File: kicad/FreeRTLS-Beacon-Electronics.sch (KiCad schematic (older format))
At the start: 28 parts

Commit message: Annotate sch
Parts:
- gave numbers to parts that had none: 28

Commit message: Add ferrite and change lib to fix ERC errors
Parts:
- added L4: L, symbol Device:L
- U3: symbol RF_Module:DWM1001 -> FreeRTLS-Beacon:DWM1001
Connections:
- wire segments 126 -> 130
- no-connect marks 52 -> 53
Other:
- moved on the sheet: C5, C6, D2, D4, J1, L1
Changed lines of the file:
@@
 $EndDescr
 $Comp
-L RF_Module:DWM1001 U3
+L FreeRTLS-Beacon:DWM1001 U3
 U 1 1 5F4EAC7B
 P 8600 3650
@@
 L Connector:USB_B_Micro J1
 U 1 1 5F4ED800
-P 900 1200
-F 0 "J1" H 957 1667 50  0000 C CNN
-F 1 "USB_B_Micro" H 957 1576 50  0000 C CNN
-F 2 "" H 1050 1150 50  0001 C CNN
-F 3 "~" H 1050 1150 50  0001 C CNN
-	1    900  1200
+P 750 1200
+F 0 "J1" H 807 1667 50  0000 C CNN
+F 1 "USB_B_Micro" H 807 1576 50  0000 C CNN
+F 2 "" H 900 1150 50  0001 C CNN
+F 3 "~" H 900 1150 50  0001 C CNN
+	1    750  1200
 	1    0    0    -1
 $EndComp
@@
 NoConn ~ 2500 5750
 NoConn ~ 2500 6950
-NoConn ~ 1200 1400
+NoConn ~ 1050 1400
 $Comp
 L Diode:PMEG3020EH D2
 U 1 1 5F4FD35F
-P 1850 1000
-F 0 "D2" H 1850 784 50  0000 C CNN
-F 1 "PMEG3020EH" H 1850 875 50  0000 C CNN
-F 2 "Diode_SMD:D_SOD-123F" H 1850 825 50  0001 C CNN
-F 3 "https://assets.nexperia.com/documents/data-sheet/PMEG3020EH_EJ.pdf" H 1850 1000 50  0001 C CNN
-	1    1850 1000
+P 1950 1000
+F 0 "D2" H 1950 784 50  0000 C CNN
+F 1 "PMEG3020EH" H 1950 875 50  0000 C CNN
+F 2 "Diode_SMD:D_SOD-123F" H 1950 825 50  0001 C CNN
+F 3 "https://assets.nexperia.com/documents/data-sheet/PMEG3020EH_EJ.pdf" H 1950 1000 50  0001 C CNN
+	1    1950 1000
 	-1   0    0    1
 $EndComp
 Wire Wire Line
-	2000 1000 2050 1000
+	2100 1000 2150 1000
 $Comp
 L Device:C C5
 U 1 1 5F4F0A23
-P 2050 1200
-F 0 "C5" H 2165 1246 50  0000 L CNN
-F 1 "C" H 2165 1155 50  0000 L CNN
-F 2 "" H 2088 1050 50  0001 C CNN
-F 3 "~" H 2050 1200 50  0001 C CNN
-	1    2050 1200
-	1    0    0    -1
-$EndComp
-Wire Wire Line
-	2050 1050 2050 1000
-Connection ~ 2050 1000
-Wire Wire Line
-	2050 1000 2400 1000
+P 2150 1200
+F 0 "C5" H 2265 1246 50  0000 L CNN
+F 1 "C" H 2265 1155 50  0000 L CNN
+F 2 "" H 2188 1050 50  0001 C CNN
+F 3 "~" H 2150 1200 50  0001 C CNN
+	1    2150 1200
+	1    0    0    -1
+$EndComp
+Wire Wire Line
+	2150 1050 2150 1000
+Connection ~ 2150 1000
+Wire Wire Line
+	2150 1000 2450 1000
 $Comp
 L power:GND #PWR09
 U 1 1 5F4F1ADF
-P 2050 1450
-F 0 "#PWR09" H 2050 1200 50  0001 C CNN
-F 1 "GND" H 2055 1277 50  0000 C CNN
-F 2 "" H 2050 1450 50  0001 C CNN
-F 3 "" H 2050 1450 50  0001 C CNN
-	1    2050 1450
-	1    0    0    -1
-$EndComp
-Wire Wire Line
-	2050 1450 2050 1350
+P 2150 1450
+F 0 "#PWR09" H 2150 1200 50  0001 C CNN
+F 1 "GND" H 2155 1277 50  0000 C CNN
+F 2 "" H 2150 1450 50  0001 C CNN
+F 3 "" H 2150 1450 50  0001 C CNN
+	1    2150 1450
+	1    0    0    -1
+$EndComp
+Wire Wire Line
+	2150 1450 2150 1350
 $Comp
 L Device:D_Zener D4
 U 1 1 5F4F2846
-P 2400 1200
-F 0 "D4" V 2354 1280 50  0000 L CNN
-F 1 "D_Zener" V 2445 1280 50  0000 L CNN
-F 2 "" H 2400 1200 50  0001 C CNN
-F 3 "~" H 2400 1200 50  0001 C CNN
-	1    2400 1200
+P 2450 1200
+F 0 "D4" V 2404 1280 50  0000 L CNN
+F 1 "D_Zener" V 2495 1280 50  0000 L CNN
+F 2 "" H 2450 1200 50  0001 C CNN
+F 3 "~" H 2450 1200 50  0001 C CNN
+	1    2450 1200
 	0    1    1    0
 $EndComp
 Wire Wire Line
-	2400 1050 2400 1000
-Connection ~ 2400 1000
+	2450 1050 2450 1000
+Connection ~ 2450 1000
 $Comp
 L Device:CP C6
 U 1 1 5F4F33A4
-P 2900 1200
-F 0 "C6" H 3018 1246 50  0000 L CNN
-F 1 "CP" H 3018 1155 50  0000 L CNN
-F 2 "" H 2938 1050 50  0001 C CNN
-F 3 "~" H 2900 1200 50  0001 C CNN
-	1    2900 1200
-	1    0    0    -1
-$EndComp
-Wire Wire Line
-	2400 1000 2900 1000
-Wire Wire Line
-	2900 1050 2900 1000
-Connection ~ 2900 1000
-Wire Wire Line
-	2900 1000 3250 1000
+P 2950 1200
+F 0 "C6" H 3068 1246 50  0000 L CNN
+F 1 "CP" H 3068 1155 50  0000 L CNN
+F 2 "" H 2988 1050 50  0001 C CNN
+F 3 "~" H 2950 1200 50  0001 C CNN
+	1    2950 1200
+	1    0    0    -1
+$EndComp
+Wire Wire Line
+	2450 1000 2950 1000
+Wire Wire Line
+	2950 1050 2950 1000
+Connection ~ 2950 1000
+Wire Wire Line
+	2950 1000 3250 1000
 $Comp
 L Device:R R2
@@
 L power:GND #PWR011
 U 1 1 5F4F9649
-P 2400 1450
-F 0 "#PWR011" H 2400 1200 50  0001 C CNN
-F 1 "GND" H 2405 1277 50  0000 C CNN
-F 2 "" H 2400 1450 50  0001 C CNN
-F 3 "" H 2400 1450 50  0001 C CNN
-	1    2400 1450
+P 2450 1450
+F 0 "#PWR011" H 2450 1200 50  0001 C CNN
+F 1 "GND" H 2455 1277 50  0000 C CNN
+F 2 "" H 2450 1450 50  0001 C CNN
+F 3 "" H 2450 1450 50  0001 C CNN
+	1    2450 1450
 	1    0    0    -1
 $EndComp
@@
 L power:GND #PWR012
 U 1 1 5F4F99D9
-P 2900 1450
-F 0 "#PWR012" H 2900 1200 50  0001 C CNN
-F 1 "GND" H 2905 1277 50  0000 C CNN
-F 2 "" H 2900 1450 50  0001 C CNN
-F 3 "" H 2900 1450 50  0001 C CNN
-	1    2900 1450
+P 2950 1450
+F 0 "#PWR012" H 2950 1200 50  0001 C CNN
+F 1 "GND" H 2955 1277 50  0000 C CNN
+F 2 "" H 2950 1450 50  0001 C CNN
+F 3 "" H 2950 1450 50  0001 C CNN
+	1    2950 1450
 	1    0    0    -1
 $EndComp
@@
 $EndComp
 Wire Wire Line
-	2400 1350 2400 1450
-Wire Wire Line
-	2900 1350 2900 1450
+	2450 1350 2450 1450
+Wire Wire Line
+	2950 1350 2950 1450
 Wire Wire Line
 	3250 1750 3250 1850
@@
 P 4700 850
 F 0 "#PWR019" H 4700 700 50  0001 C CNN
-F 1 "+3V3" H 4715 1023 50  0000 C CNN
+F 1 "+3V3" H 4650 1000 50  0000 C CNN
 F 2 "" H 4700 850 50  0001 C CNN
 F 3 "" H 4700 850 50  0001 C CNN
@@
 L power:GND #PWR01
 U 1 1 5F50CB2D
-P 800 1700
-F 0 "#PWR01" H 800 1450 50  0001 C CNN
-F 1 "GND" H 805 1527 50  0000 C CNN
-F 2 "" H 800 1700 50  0001 C CNN
-F 3 "" H 800 1700 50  0001 C CNN
-	1    800  1700
-	1    0    0    -1
-$EndComp
-Wire Wire Line
-	800  1600 800  1650
-Wire Wire Line
-	900  1650 800  1650
-Connection ~ 800  1650
-Wire Wire Line
-	800  1650 800  1700
-Wire Wire Line
-	900  1600 900  1650
+P 750 2100
+F 0 "#PWR01" H 750 1850 50  0001 C CNN
+F 1 "GND" H 755 1927 50  0000 C CNN
+F 2 "" H 750 2100 50  0001 C CNN
+F 3 "" H 750 2100 50  0001 C CNN
+	1    750  2100
+	1    0    0    -1
+$EndComp
 $Comp
 L power:GND #PWR014
@@
 L Device:L L1
 U 1 1 5F5536AE
-P 1500 1000
-F 0 "L1" V 1690 1000 50  0000 C CNN
-F 1 "L" V 1599 1000 50  0000 C CNN
-F 2 "" H 1500 1000 50  0001 C CNN
-F 3 "~" H 1500 1000 50  0001 C CNN
-	1    1500 1000
+P 1600 1000
+F 0 "L1" V 1790 1000 50  0000 C CNN
+F 1 "L" V 1699 1000 50  0000 C CNN
+F 2 "" H 1600 1000 50  0001 C CNN
+F 3 "~" H 1600 1000 50  0001 C CNN
+	1    1600 1000
 	0    -1   -1   0
 $EndComp
-Wire Wire Line
-	1200 1000 1300 1000
 $Comp
 L power:VBUS #PWR07
@@
 L power:VBUS #PWR04
 U 1 1 5F55F950
-P 1300 800
-F 0 "#PWR04" H 1300 650 50  0001 C CNN
-F 1 "VBUS" H 1315 973 50  0000 C CNN
-F 2 "" H 1300 800 50  0001 C CNN
-F 3 "" H 1300 800 50  0001 C CNN
-	1    1300 800
-	1    0    0    -1
-$EndComp
-Wire Wire Line
-	1650 1000 1700 1000
-Wire Wire Line
-	1300 800  1300 1000
-Connection ~ 1300 1000
-Wire Wire Line
-	1300 1000 1350 1000
+P 1400 800
+F 0 "#PWR04" H 1400 650 50  0001 C CNN
+F 1 "VBUS" H 1415 973 50  0000 C CNN
+F 2 "" H 1400 800 50  0001 C CNN
+F 3 "" H 1400 800 50  0001 C CNN
+	1    1400 800
+	1    0    0    -1
+$EndComp
+Wire Wire Line
+	1750 1000 1800 1000
+Wire Wire Line
+	1400 800  1400 1000
+Connection ~ 1400 1000
+Wire Wire Line
+	1400 1000 1450 1000
 $Comp
 L Device:L_Core_Iron_Coupled_1243 L2
@@
 	1800 1200 1800 1550
 Wire Wire Line
-	1200 1200 1800 1200
+	1050 1200 1800 1200
 Wire Wire Line
 	1600 1300 1600 1550
 Wire Wire Line
-	1200 1300 1600 1300
+	1050 1300 1600 1300
 Wire Wire Line
 	1200 2800 1150 2800
@@
 DecaWave DWM1001
 Wire Notes Line
-	5150 3650 500  3650
+	5250 3650 500  3650
 Wire Notes Line
-	5150 500  5150 7750
+	5250 500  5250 7750
+Wire Wire Line
+	1050 1000 1400 1000
+$Comp
+L power:PWR_FLAG #FLG0101
+U 1 1 5F7CC472
+P 3250 850
+F 0 "#FLG0101" H 3250 925 50  0001 C CNN
+F 1 "PWR_FLAG" H 3250 1023 50  0000 C CNN
+F 2 "" H 3250 850 50  0001 C CNN
+F 3 "~" H 3250 850 50  0001 C CNN
+	1    3250 850
+	1    0    0    -1
+$EndComp
+Wire Wire Line
+	3250 850  3250 1000
+$Comp
+L power:PWR_FLAG #FLG0102
+U 1 1 5F7D1FCE
+P 5000 850
+F 0 "#FLG0102" H 5000 925 50  0001 C CNN
+F 1 "PWR_FLAG" H 5000 1023 50  0000 C CNN
+F 2 "" H 5000 850 50  0001 C CNN
+F 3 "~" H 5000 850 50  0001 C CNN
+	1    5000 850
+	1    0    0    -1
+$EndComp
+Wire Wire Line
+	5000 850  5000 1000
+Wire Wire Line
+	5000 1000 4700 1000
+Connection ~ 4700 1000
+NoConn ~ 2250 5550
+$Comp
+L Device:L L4
+U 1 1 5F7E7895
+P 650 1800
+F 0 "L4" H 703 1754 50  0000 L CNN
+F 1 "L" H 703 1845 50  0000 L CNN
+F 2 "" H 650 1800 50  0001 C CNN
+F 3 "~" H 650 1800 50  0001 C CNN
+	1    650  1800
+	-1   0    0    1
+$EndComp
+Wire Wire Line
+	750  1600 750  2050
+Wire Wire Line
+	650  1600 650  1650
+Wire Wire Line
+	650  1950 650  2050
+Wire Wire Line
+	650  2050 750  2050
+Connection ~ 750  2050
+Wire Wire Line
+	750  2050 750  2100
 $EndSCHEMATC

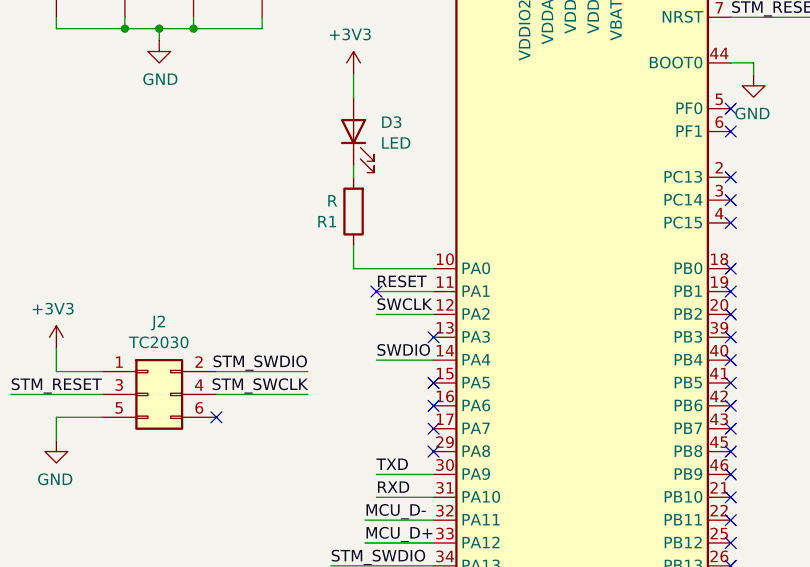
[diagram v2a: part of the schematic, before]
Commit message: Delete reset label
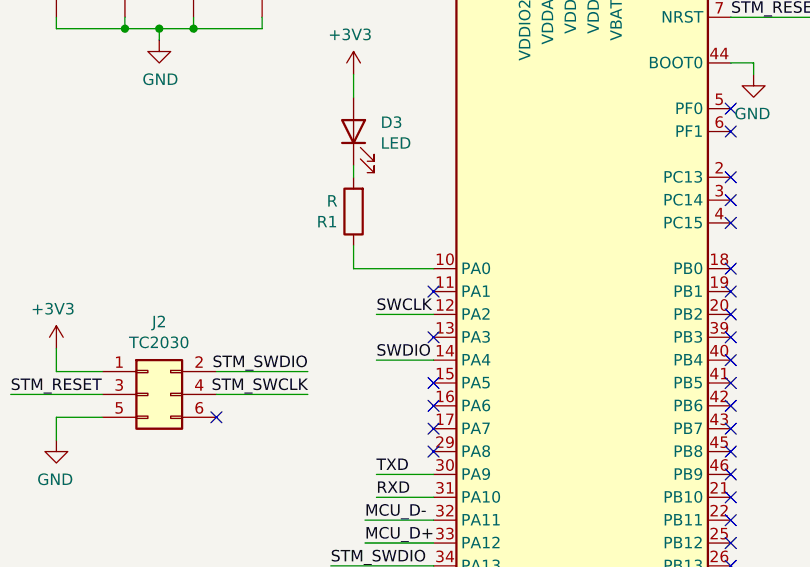
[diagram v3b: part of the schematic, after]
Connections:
- net RESET: no longer names the net of U1.11 (PA1)
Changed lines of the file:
@@
 	3900 4550 3900 4600
 Wire Wire Line
-	2250 5550 2500 5550
-Wire Wire Line
 	2250 5650 2500 5650
 Wire Wire Line
 	2500 5850 2250 5850
-Text Label 2250 5550 0    50   ~ 0
-RESET
 Text Label 2250 5650 0    50   ~ 0
 SWCLK
@@
 	5000 1000 4700 1000
 Connection ~ 4700 1000
-NoConn ~ 2250 5550
+NoConn ~ 2500 5550
 $Comp
 L Device:L L4

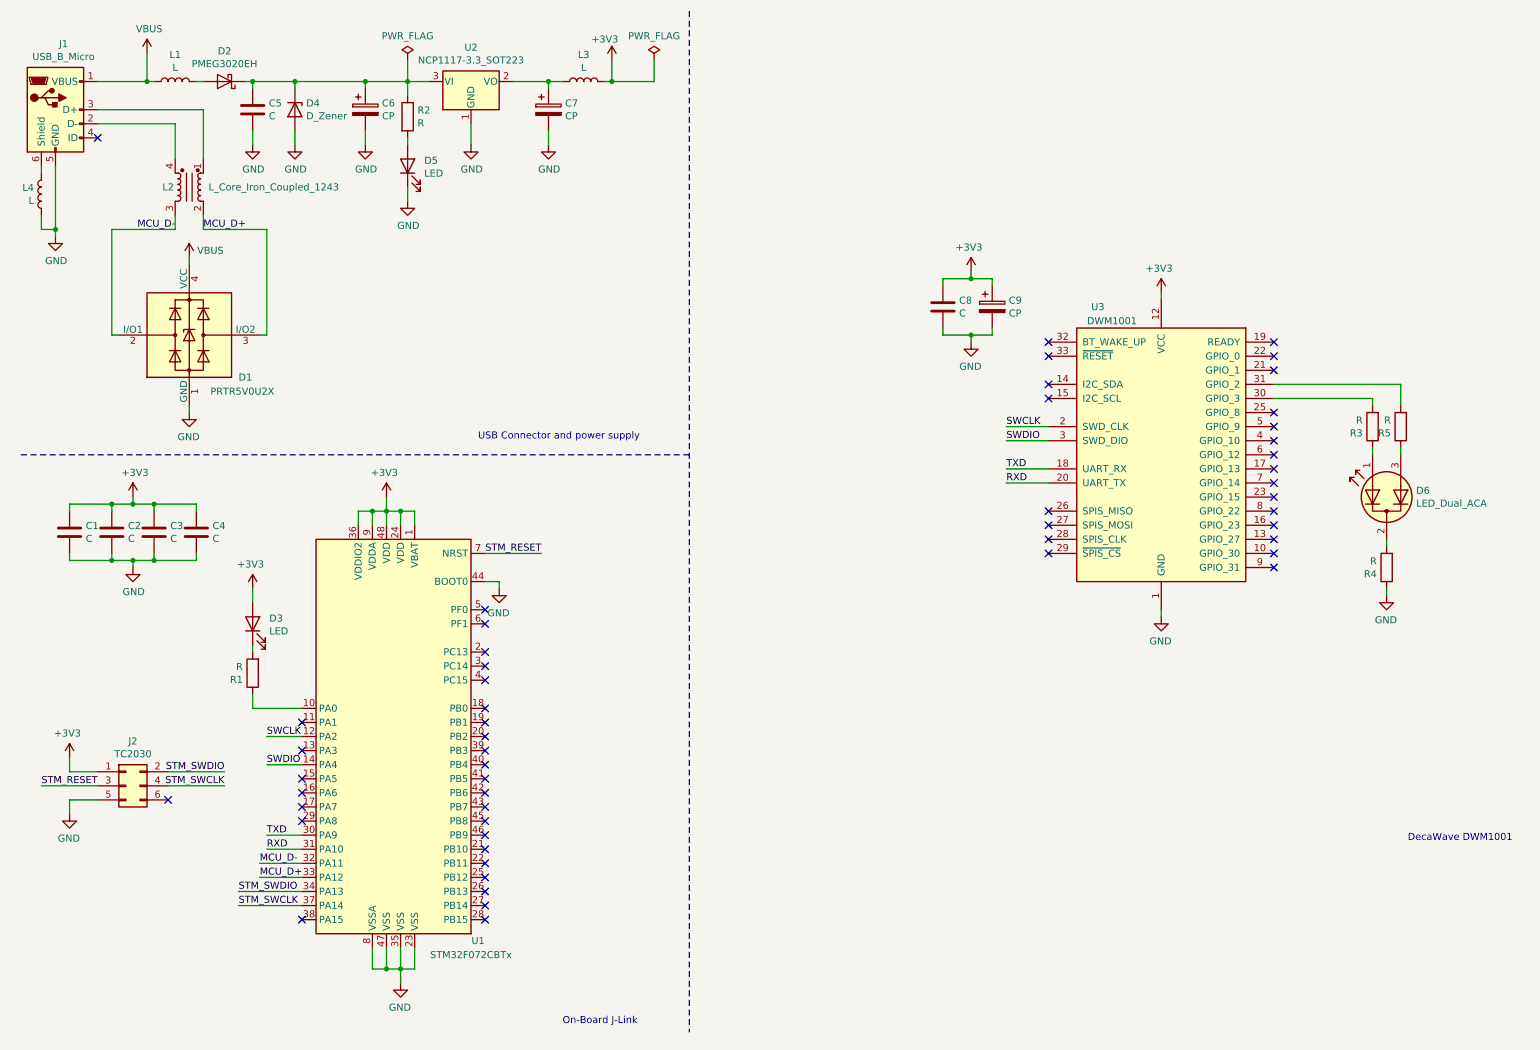
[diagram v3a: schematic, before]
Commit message: Update values and order power supply
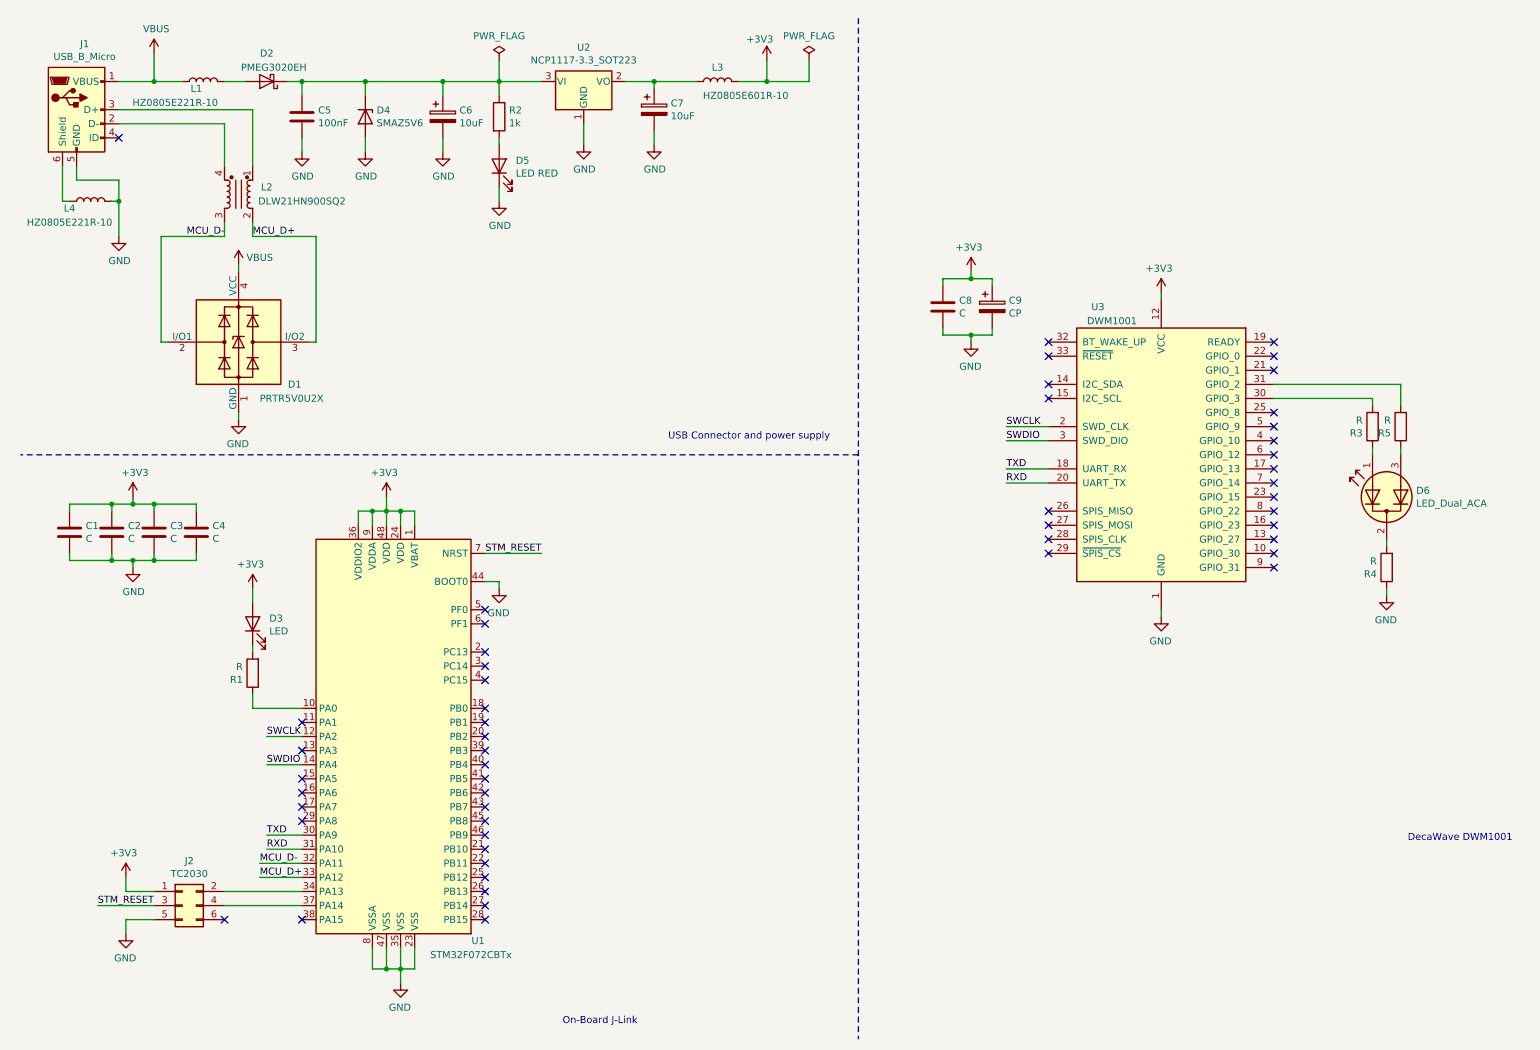
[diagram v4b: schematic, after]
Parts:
- C5: value C -> 100nF
- C6, C7: value CP -> 10uF
- D4: value D_Zener -> SMAZ5V6
- D5: value LED -> LED RED
- L1, L4: value L -> HZ0805E221R-10
- L2: value L_Core_Iron_Coupled_1243 -> DLW21HN900SQ2
- L3: value L -> HZ0805E601R-10
- R2: value R -> 1k
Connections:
- net GND: now also L4.2; no longer L4.1
- net at J1.6 (Shield): now also L4.1; no longer L4.2
- net STM_SWCLK: no longer names the net of J2.4 (Pin_4), U1.37 (PA14)
- net STM_SWDIO: no longer names the net of J2.2 (Pin_2), U1.34 (PA13)
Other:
- moved on the sheet: C5, C6, C7, D1, D2, D4, D5, J1, J2, L1, L2, L3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
